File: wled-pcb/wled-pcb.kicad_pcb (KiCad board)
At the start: 2 copper layers, 90.2 x 90.2 mm, 36 parts, among them J2 Conn_02x03_Counter_Clockwise, J3 Screw_Terminal_01x03, J4 Screw_Terminal_01x03, J5 Screw_Terminal_01x03, J6 Screw_Terminal_01x02, J7 Screw_Terminal_01x03, K1 Relay_SPDT, Q1 BC337, SW1 SW_Push, SW2 SW_Push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

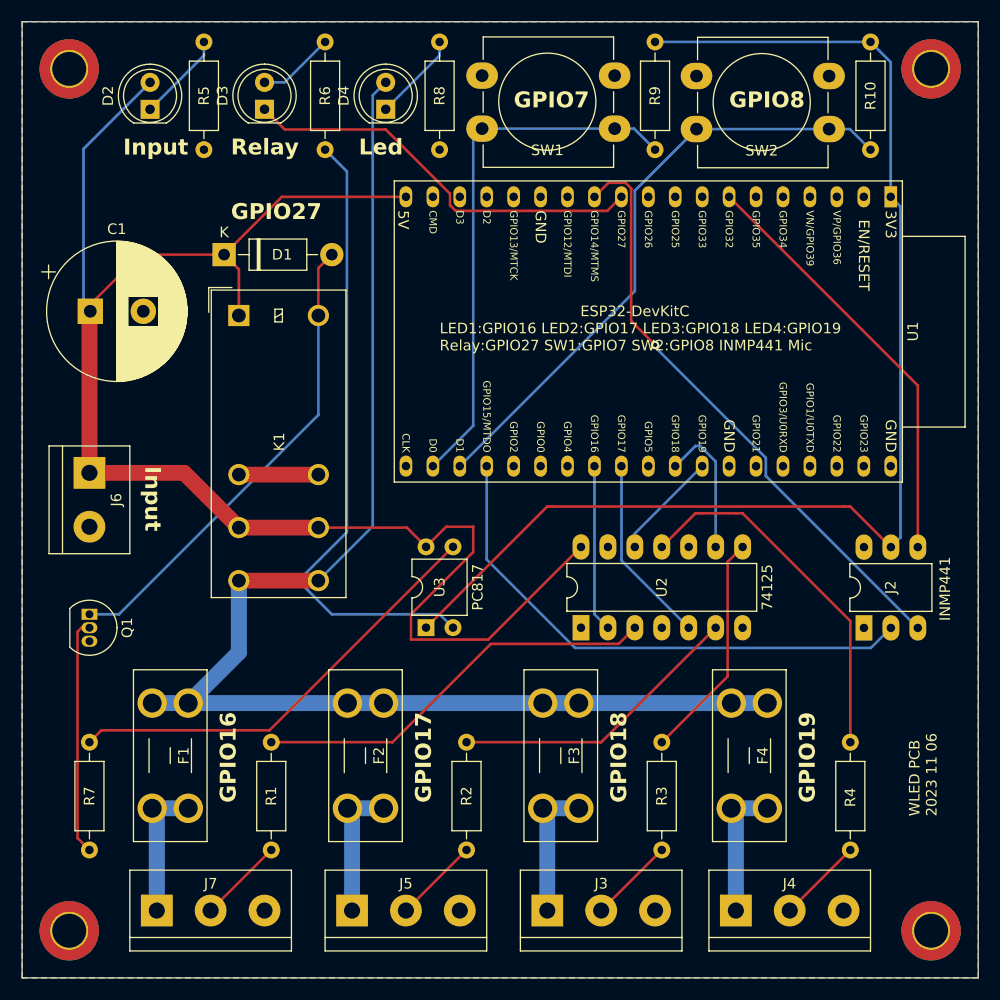
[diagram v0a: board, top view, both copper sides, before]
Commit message: use different pins for switches
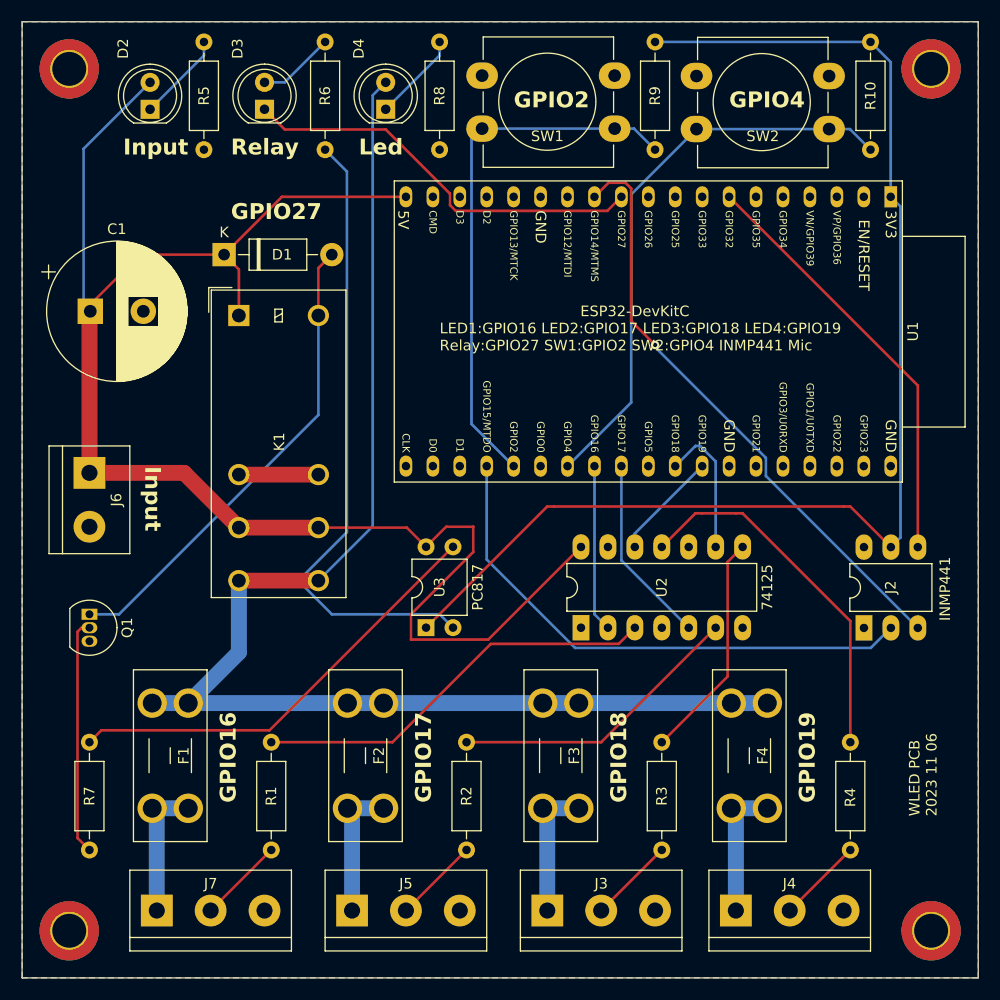
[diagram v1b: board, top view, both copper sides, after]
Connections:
- U1 pad 21: /sw 1 -> unconnected-(U1-SD_DATA0/GPIO7-Pad21)
- U1 pad 22: /sw 2 -> unconnected-(U1-SD_DATA1/GPIO8-Pad22)
- U1 pad 24: unconnected-(U1-ADC2_CH2/GPIO2-Pad24) -> /sw 1
- U1 pad 26: unconnected-(U1-ADC2_CH0/GPIO4-Pad26) -> /sw 2
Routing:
- net /sw 2: track 58.3 -> 54.0 mm
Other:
- board text added: "GPIO2"
- board text added: "GPIO4"
- board text added: "LED1:GPIO16 LED2:GPIO17 LED3:GPIO18 LED4:GPIO19 Relay:GPIO27 SW1:GPIO2 SW2:GPIO4 INMP441 Mic"
- board text removed: "GPIO7"
- board text removed: "GPIO8"
- board text removed: "LED1:GPIO16 LED2:GPIO17 LED3:GPIO18 LED4:GPIO19 Relay:GPIO27 SW1:GPIO7 SW2:GPIO8 INMP441 Mic"
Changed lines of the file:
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@@
   (net 42 "/led1 lo")
   (net 43 "/led2 lo")
-  (net 44 "unconnected-(U1-ADC2_CH2{slash}GPIO2-Pad24)")
+  (net 44 "unconnected-(U1-SD_DATA0{slash}GPIO7-Pad21)")
   (net 45 "unconnected-(U1-GPIO0{slash}BOOT{slash}ADC2_CH1-Pad25)")
-  (net 46 "unconnected-(U1-ADC2_CH0{slash}GPIO4-Pad26)")
+  (net 46 "unconnected-(U1-SD_DATA1{slash}GPIO8-Pad22)")
   (net 47 "unconnected-(U1-SD_DATA2{slash}GPIO9-Pad16)")
   (net 48 "unconnected-(U1-SD_CLK{slash}GPIO6-Pad20)")
@@
       (net 48 "unconnected-(U1-SD_CLK{slash}GPIO6-Pad20)") (pinfunction "SD_CLK/GPIO6") (pintype "bidirectional"))
     (pad "21" thru_hole oval (at 25.39632 43.17728 180) (size 1.2 2) (drill 0.8) (layers "*.Cu" "*.Mask")
-      (net 50 "/sw 1") (pinfunction "SD_DATA0/GPIO7") (pintype "bidirectional"))
+      (net 44 "unconnected-(U1-SD_DATA0{slash}GPIO7-Pad21)") (pinfunction "SD_DATA0/GPIO7") (pintype "bidirectional"))
     (pad "22" thru_hole oval (at 25.4 40.64 180) (size 1.2 2) (drill 0.8) (layers "*.Cu" "*.Mask")
-      (net 57 "/sw 2") (pinfunction "SD_DATA1/GPIO8") (pintype "bidirectional"))
+      (net 46 "unconnected-(U1-SD_DATA1{slash}GPIO8-Pad22)") (pinfunction "SD_DATA1/GPIO8") (pintype "bidirectional"))
     (pad "23" thru_hole oval (at 25.4 38.1 180) (size 1.2 2) (drill 0.8) (layers "*.Cu" "*.Mask")
       (net 13 "/mic ws") (pinfunction "MTDO/GPIO15/ADC2_CH3") (pintype "bidirectional"))
     (pad "24" thru_hole oval (at 25.4 35.56 180) (size 1.2 2) (drill 0.8) (layers "*.Cu" "*.Mask")
-      (net 44 "unconnected-(U1-ADC2_CH2{slash}GPIO2-Pad24)") (pinfunction "ADC2_CH2/GPIO2") (pintype "bidirectional"))
+      (net 50 "/sw 1") (pinfunction "ADC2_CH2/GPIO2") (pintype "bidirectional"))
     (pad "25" thru_hole oval (at 25.4 33.02 180) (size 1.2 2) (drill 0.8) (layers "*.Cu" "*.Mask")
       (net 45 "unconnected-(U1-GPIO0{slash}BOOT{slash}ADC2_CH1-Pad25)") (pinfunction "GPIO0/BOOT/ADC2_CH1") (pintype "bidirectional"))
     (pad "26" thru_hole oval (at 25.4 30.48 180) (size 1.2 2) (drill 0.8) (layers "*.Cu" "*.Mask")
-      (net 46 "unconnected-(U1-ADC2_CH0{slash}GPIO4-Pad26)") (pinfunction "ADC2_CH0/GPIO4") (pintype "bidirectional"))
+      (net 57 "/sw 2") (pinfunction "ADC2_CH0/GPIO4") (pintype "bidirectional"))
     (pad "27" thru_hole oval (at 25.4 27.94 180) (size 1.2 2) (drill 0.8) (layers "*.Cu" "*.Mask")
       (net 42 "/led1 lo") (pinfunction "GPIO16") (pintype "bidirectional"))
@@
     (property "ki_keywords" "switch normally-open pushbutton push-button")
     (attr through_hole)
-    (fp_text reference "SW1" (at 6.35 -2.03905 180) (layer "F.SilkS")
+    (fp_text reference "SW1" (at 6.35 -0.715 180) (layer "F.SilkS")
         (effects (font (size 1 1) (thickness 0.15)))
     )
@@
     (property "ki_keywords" "switch normally-open pushbutton push-button")
     (attr through_hole)
-    (fp_text reference "SW2" (at 6.35 -2.03905 180) (layer "F.SilkS")
+    (fp_text reference "SW2" (at 6.25 -0.675 180) (layer "F.SilkS")
         (effects (font (size 1 1) (thickness 0.15)))
     )
@@
     (property "ki_keywords" "LED diode")
     (attr through_hole)
-    (fp_text reference "D2" (at 1.27 -3.96 90) (layer "F.SilkS")
+    (fp_text reference "D2" (at 5.72 -2.54 90) (layer "F.SilkS")
         (effects (font (size 1 1) (thickness 0.15)))
     )
@@
     (property "ki_keywords" "LED diode")
     (attr through_hole)
-    (fp_text reference "D4" (at 1.27 -3.96 90) (layer "F.SilkS")
+    (fp_text reference "D4" (at 5.715 -2.54 90) (layer "F.SilkS")
         (effects (font (size 1 1) (thickness 0.15)))
     )
@@
     (property "ki_keywords" "LED diode")
     (attr through_hole)
-    (fp_text reference "D3" (at 1.27 -3.96 90) (layer "F.SilkS")
+    (fp_text reference "D3" (at 5.715 -2.54 90) (layer "F.SilkS")
         (effects (font (size 1 1) (thickness 0.15)))
     )
@@
   (gr_rect (start 94.615 53.34) (end 184.785 143.51)
     (stroke (width 0.1) (type default)) (fill none) (layer "Edge.Cuts"))
-  (gr_text "GPIO7" (at 140.97 61.595) (layer "F.SilkS")
+  (gr_text "GPIO2" (at 140.97 61.595) (layer "F.SilkS")
     (effects (font (size 1.5 1.5) (thickness 0.3) bold) (justify left bottom))
   )
@@
     (effects (font (size 1 1) (thickness 0.15)) (justify left bottom))
   )
-  (gr_text "GPIO8" (at 161.29 61.595) (layer "F.SilkS")
+  (gr_text "GPIO4" (at 161.29 61.595) (layer "F.SilkS")
     (effects (font (size 1.5 1.5) (thickness 0.3) bold) (justify left bottom))
   )
@@
     (effects (font (size 1 1) (thickness 0.15)) (justify left bottom))
   )
-  (gr_text "LED1:GPIO16 LED2:GPIO17 LED3:GPIO18 LED4:GPIO19\nRelay:GPIO27 SW1:GPIO7 SW2:GPIO8 INMP441 Mic" (at 133.985 84.455) (layer "F.SilkS")
+  (gr_text "LED1:GPIO16 LED2:GPIO17 LED3:GPIO18 LED4:GPIO19\nRelay:GPIO27 SW1:GPIO2 SW2:GPIO4 INMP441 Mic" (at 133.985 84.455) (layer "F.SilkS")
     (effects (font (size 1 1) (thickness 0.15)) (justify left bottom))
   )
@@
   (segment (start 157.48 110.49) (end 151.13 104.14) (width 0.25) (layer "B.Cu") (net 43))
   (segment (start 150.495 63.42) (end 152.32 63.42) (width 0.25) (layer "B.Cu") (net 50))
-  (segment (start 137.16 64.255) (end 137.995 63.42) (width 0.25) (layer "B.Cu") (net 50))
+  (segment (start 137.995 63.42) (end 136.996104 64.418896) (width 0.25) (layer "B.Cu") (net 50))
   (segment (start 137.995 63.42) (end 150.495 63.42) (width 0.25) (layer "B.Cu") (net 50))
+  (segment (start 136.996104 91.276104) (end 140.97 95.25) (width 0.25) (layer "B.Cu") (net 50))
+  (segment (start 136.996104 64.418896) (end 136.996104 91.276104) (width 0.25) (layer "B.Cu") (net 50))
   (segment (start 152.32 63.42) (end 154.305 65.405) (width 0.25) (layer "B.Cu") (net 50))
-  (segment (start 133.35272 95.24632) (end 137.16 91.43904) (width 0.25) (layer "B.Cu") (net 50))
-  (segment (start 137.16 91.43904) (end 137.16 64.255) (width 0.25) (layer "B.Cu") (net 50))
   (segment (start 158.115 93.345) (end 156.21 95.25) (width 0.25) (layer "B.Cu") (net 56))
   (segment (start 160.02 102.87) (end 160.02 94.811852) (width 0.25) (layer "B.Cu") (net 56))
   (segment (start 160.02 94.811852) (end 158.553148 93.345) (width 0.25) (layer "B.Cu") (net 56))
   (segment (start 158.553148 93.345) (end 158.115 93.345) (width 0.25) (layer "B.Cu") (net 56))
+  (segment (start 152.055 89.245) (end 146.05 95.25) (width 0.25) (layer "B.Cu") (net 57))
   (segment (start 158.215 63.46) (end 170.715 63.46) (width 0.25) (layer "B.Cu") (net 57))
   (segment (start 170.715 63.46) (end 172.68 63.46) (width 0.25) (layer "B.Cu") (net 57))
-  (segment (start 158.215 63.46) (end 152.4 69.275) (width 0.25) (layer "B.Cu") (net 57))
-  (segment (start 152.4 78.74) (end 135.89 95.25) (width 0.25) (layer "B.Cu") (net 57))
+  (segment (start 152.055 69.62) (end 152.055 89.245) (width 0.25) (layer "B.Cu") (net 57))
   (segment (start 172.68 63.46) (end 174.625 65.405) (width 0.25) (layer "B.Cu") (net 57))
-  (segment (start 152.4 69.275) (end 152.4 78.74) (width 0.25) (layer "B.Cu") (net 57))
+  (segment (start 158.215 63.46) (end 152.055 69.62) (width 0.25) (layer "B.Cu") (net 57))
   (zone (net 2) (net_name "GND") (layers "F&B.Cu") (hatch edge 0.5)
     (connect_pads (clearance 0.5))

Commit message: 3.6mm trace should give 6A@1oz and 10A@2oz
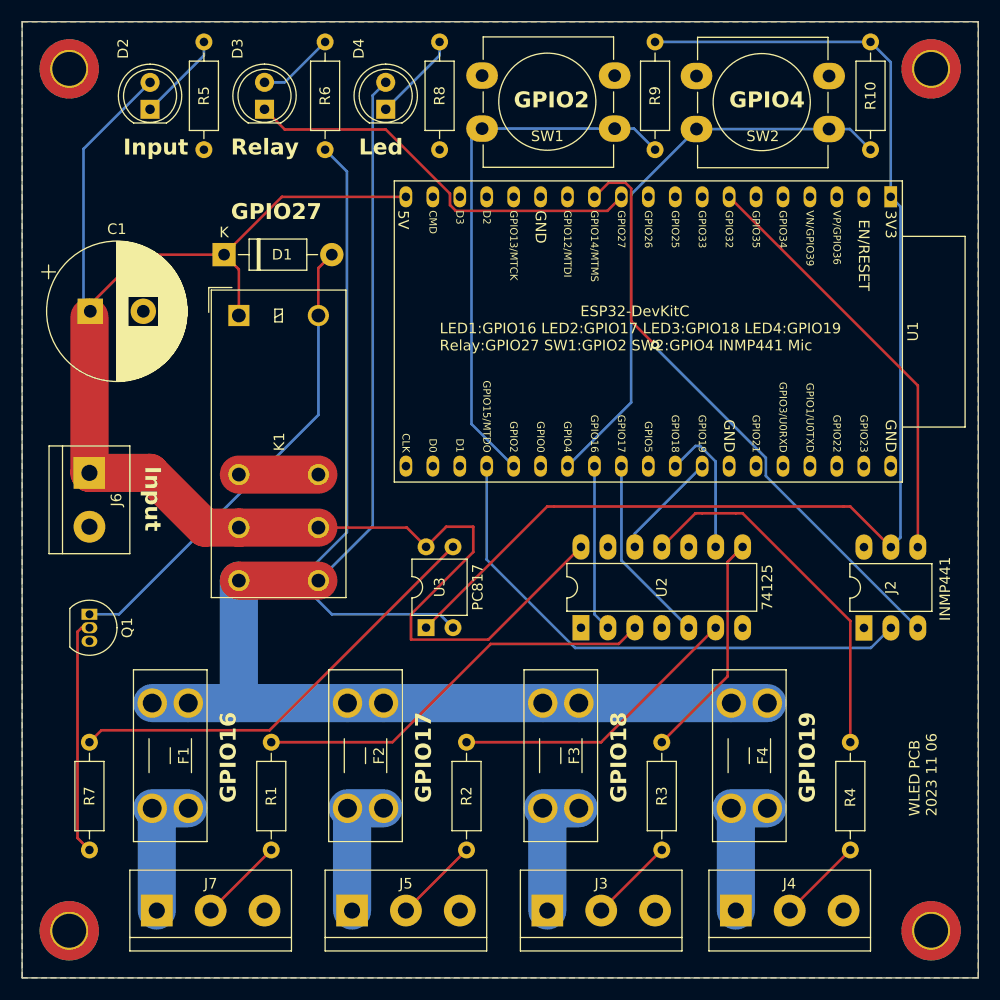
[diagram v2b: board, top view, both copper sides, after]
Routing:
- net /5v sw: track 128.7 -> 126.7 mm
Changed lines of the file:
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@@
     (effects (font (size 1 1) (thickness 0.15)) (justify left bottom))
   )
-  (segment (start 100.965 95.885) (end 109.895 95.885) (width 1.5) (layer "F.Cu") (net 1))
   (segment (start 122.555 101.045) (end 130.895 101.045) (width 0.25) (layer "F.Cu") (net 1))
   (segment (start 115.055 81.045) (end 115.055 76.695) (width 0.25) (layer "F.Cu") (net 1))
   (segment (start 138.585 111.605) (end 131.29 111.605) (width 0.25) (layer "F.Cu") (net 1))
   (segment (start 130.81 69.85) (end 119.115 69.85) (width 0.25) (layer "F.Cu") (net 1))
+  (segment (start 111.84 101.045) (end 106.68 95.885) (width 3.6) (layer "F.Cu") (net 1))
   (segment (start 147.32 102.87) (end 138.585 111.605) (width 0.25) (layer "F.Cu") (net 1))
   (segment (start 105.7525 75.3025) (end 113.6625 75.3025) (width 0.25) (layer "F.Cu") (net 1))
-  (segment (start 109.895 95.885) (end 115.055 101.045) (width 1.5) (layer "F.Cu") (net 1))
   (segment (start 100.965 81.2) (end 100.41 80.645) (width 0.25) (layer "F.Cu") (net 1))
   (segment (start 137.16 100.965) (end 137.16 103.35) (width 0.25) (layer "F.Cu") (net 1))
+  (segment (start 115.055 101.045) (end 111.84 101.045) (width 3.6) (layer "F.Cu") (net 1))
   (segment (start 137.16 103.35) (end 131.29 109.22) (width 0.25) (layer "F.Cu") (net 1))
   (segment (start 115.055 76.695) (end 113.6625 75.3025) (width 0.25) (layer "F.Cu") (net 1))
   (segment (start 131.29 111.605) (end 131.29 109.22) (width 0.25) (layer "F.Cu") (net 1))
   (segment (start 100.41 80.645) (end 105.7525 75.3025) (width 0.25) (layer "F.Cu") (net 1))
-  (segment (start 122.555 101.045) (end 115.055 101.045) (width 1.5) (layer "F.Cu") (net 1))
+  (segment (start 122.555 101.045) (end 115.055 101.045) (width 3.6) (layer "F.Cu") (net 1))
   (segment (start 134.605 100.965) (end 137.16 100.965) (width 0.25) (layer "F.Cu") (net 1))
   (segment (start 132.71 102.86) (end 134.605 100.965) (width 0.25) (layer "F.Cu") (net 1))
   (segment (start 130.895 101.045) (end 132.71 102.86) (width 0.25) (layer "F.Cu") (net 1))
   (segment (start 119.115 69.85) (end 113.6625 75.3025) (width 0.25) (layer "F.Cu") (net 1))
-  (segment (start 100.965 95.885) (end 100.965 81.2) (width 1.5) (layer "F.Cu") (net 1))
+  (segment (start 100.965 95.885) (end 100.965 81.2) (width 3.6) (layer "F.Cu") (net 1))
+  (segment (start 106.68 95.885) (end 100.965 95.885) (width 3.6) (layer "F.Cu") (net 1))
   (segment (start 106.68 59.06) (end 100.41 65.33) (width 0.25) (layer "B.Cu") (net 1))
   (segment (start 100.41 65.33) (end 100.41 80.645) (width 0.25) (layer "B.Cu") (net 1))
@@
   (segment (start 128.905 61.595) (end 133.985 56.515) (width 0.25) (layer "B.Cu") (net 7))
   (segment (start 133.985 56.515) (end 133.985 55.245) (width 0.25) (layer "B.Cu") (net 7))
-  (segment (start 122.555 106.045) (end 115.055 106.045) (width 1.5) (layer "F.Cu") (net 8))
-  (segment (start 147.115 117.595) (end 161.495 117.595) (width 1.5) (layer "B.Cu") (net 8))
+  (segment (start 122.555 106.045) (end 115.055 106.045) (width 3.6) (layer "F.Cu") (net 8))
+  (segment (start 115.055 106.045) (end 115.055 117.475) (width 3.6) (layer "B.Cu") (net 8))
+  (segment (start 147.115 117.595) (end 161.495 117.595) (width 3.6) (layer "B.Cu") (net 8))
   (segment (start 122.555 106.045) (end 127.68 100.92) (width 0.25) (layer "B.Cu") (net 8))
   (segment (start 127.68 100.92) (end 127.68 60.28) (width 0.25) (layer "B.Cu") (net 8))
   (segment (start 127.68 60.28) (end 128.905 59.055) (width 0.25) (layer "B.Cu") (net 8))
-  (segment (start 161.495 117.595) (end 164.895 117.595) (width 1.5) (layer "B.Cu") (net 8))
-  (segment (start 110.285 117.595) (end 125.3 117.595) (width 1.5) (layer "B.Cu") (net 8))
-  (segment (start 115.055 106.045) (end 115.055 112.825) (width 1.5) (layer "B.Cu") (net 8))
-  (segment (start 143.715 117.595) (end 147.115 117.595) (width 1.5) (layer "B.Cu") (net 8))
-  (segment (start 106.885 117.595) (end 110.285 117.595) (width 1.5) (layer "B.Cu") (net 8))
-  (segment (start 128.7 117.595) (end 143.715 117.595) (width 1.5) (layer "B.Cu") (net 8))
-  (segment (start 115.055 112.825) (end 110.285 117.595) (width 1.5) (layer "B.Cu") (net 8))
-  (segment (start 125.3 117.595) (end 128.7 117.595) (width 1.5) (layer "B.Cu") (net 8))
-  (segment (start 110.285 127.515) (end 106.885 127.515) (width 1.5) (layer "B.Cu") (net 9))
-  (segment (start 107.315 137.16) (end 107.315 127.945) (width 1.5) (layer "B.Cu") (net 9))
+  (segment (start 110.285 117.595) (end 114.935 117.595) (width 3.6) (layer "B.Cu") (net 8))
+  (segment (start 161.495 117.595) (end 164.895 117.595) (width 3.6) (layer "B.Cu") (net 8))
+  (segment (start 114.935 117.595) (end 125.3 117.595) (width 3.6) (layer "B.Cu") (net 8))
+  (segment (start 143.715 117.595) (end 147.115 117.595) (width 3.6) (layer "B.Cu") (net 8))
+  (segment (start 106.885 117.595) (end 110.285 117.595) (width 3.6) (layer "B.Cu") (net 8))
+  (segment (start 128.7 117.595) (end 143.715 117.595) (width 3.6) (layer "B.Cu") (net 8))
+  (segment (start 115.055 117.475) (end 114.935 117.595) (width 1.5) (layer "B.Cu") (net 8))
+  (segment (start 125.3 117.595) (end 128.7 117.595) (width 3.6) (layer "B.Cu") (net 8))
+  (segment (start 110.285 127.515) (end 106.885 127.515) (width 3.6) (layer "B.Cu") (net 9))
+  (segment (start 107.315 137.16) (end 107.315 127.945) (width 3.6) (layer "B.Cu") (net 9))
   (segment (start 107.315 127.945) (end 106.885 127.515) (width 0.25) (layer "B.Cu") (net 9))
-  (segment (start 125.73 137.16) (end 125.73 127.945) (width 1.5) (layer "B.Cu") (net 10))
-  (segment (start 128.7 127.515) (end 125.3 127.515) (width 1.5) (layer "B.Cu") (net 10))
+  (segment (start 125.73 137.16) (end 125.73 127.945) (width 3.6) (layer "B.Cu") (net 10))
+  (segment (start 128.7 127.515) (end 125.3 127.515) (width 3.6) (layer "B.Cu") (net 10))
   (segment (start 125.73 127.945) (end 125.3 127.515) (width 0.25) (layer "B.Cu") (net 10))
-  (segment (start 147.115 127.515) (end 143.715 127.515) (width 1.5) (layer "B.Cu") (net 11))
-  (segment (start 144.145 137.16) (end 144.145 127.945) (width 1.5) (layer "B.Cu") (net 11))
+  (segment (start 147.115 127.515) (end 143.715 127.515) (width 3.6) (layer "B.Cu") (net 11))
+  (segment (start 144.145 137.16) (end 144.145 127.945) (width 3.6) (layer "B.Cu") (net 11))
   (segment (start 144.145 127.945) (end 143.715 127.515) (width 0.25) (layer "B.Cu") (net 11))
   (segment (start 161.925 127.945) (end 161.495 127.515) (width 0.25) (layer "B.Cu") (net 12))
-  (segment (start 164.895 127.515) (end 161.495 127.515) (width 1.5) (layer "B.Cu") (net 12))
-  (segment (start 161.925 137.16) (end 161.925 127.945) (width 1.5) (layer "B.Cu") (net 12))
+  (segment (start 164.895 127.515) (end 161.495 127.515) (width 3.6) (layer "B.Cu") (net 12))
+  (segment (start 161.925 137.16) (end 161.925 127.945) (width 3.6) (layer "B.Cu") (net 12))
   (segment (start 138.43 95.25) (end 138.43 104.05962) (width 0.25) (layer "B.Cu") (net 13))
   (segment (start 146.76538 112.395) (end 174.655 112.395) (width 0.25) (layer "B.Cu") (net 13))
@@
   (segment (start 130.81 137.16) (end 136.525 131.445) (width 0.25) (layer "F.Cu") (net 19))
   (segment (start 112.395 137.16) (end 118.11 131.445) (width 0.25) (layer "F.Cu") (net 20))
-  (segment (start 122.555 96.045) (end 115.055 96.045) (width 1.5) (layer "F.Cu") (net 21))
+  (segment (start 122.555 96.045) (end 115.055 96.045) (width 3.6) (layer "F.Cu") (net 21))
   (segment (start 99.84 110.868675) (end 100.218675 110.49) (width 0.25) (layer "F.Cu") (net 22))
   (segment (start 100.218675 110.49) (end 100.965 110.49) (width 0.25) (layer "F.Cu") (net 22))
